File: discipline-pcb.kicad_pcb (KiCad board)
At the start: 2 copper layers, 304.9 x 122.8 mm, 197 parts, among them J1 AVR-ISP-6, SW1 KEYSW, SW10 KEYSW, SW11 KEYSW, SW12 KEYSW, SW13 KEYSW, SW14 KEYSW, SW15 KEYSW, SW16 KEYSW, SW17 KEYSW, SW18 KEYSW, SW19 KEYSW, SW2 KEYSW, SW20 KEYSW, SW21 KEYSW, SW22 KEYSW, SW23 KEYSW, SW24 KEYSW, SW25 KEYSW, SW26 KEYSW, SW27 KEYSW, SW28 KEYSW, SW29 KEYSW, SW3 KEYSW, SW30 KEYSW, SW31 KEYSW, SW32 KEYSW, SW33 KEYSW, SW34 KEYSW, SW35 KEYSW, SW36 KEYSW, SW37 KEYSW, SW38 KEYSW, SW39 KEYSW, SW4 KEYSW, SW40 KEYSW, SW41 KEYSW, SW42 KEYSW, SW43 KEYSW, SW44 KEYSW, SW45 KEYSW, SW46 KEYSW, SW47 KEYSW, SW48 KEYSW, SW49 KEYSW, SW5 KEYSW, SW50 KEYSW, SW51 KEYSW, SW52 KEYSW, SW53 KEYSW, SW54 KEYSW, SW55 KEYSW, SW56 KEYSW, SW57 KEYSW, SW58 KEYSW, SW59 KEYSW, SW6 KEYSW, SW60 KEYSW, SW61 KEYSW, SW62 KEYSW, SW63 KEYSW, SW64 KEYSW, SW65 KEYSW, SW66 KEYSW, SW67 KEYSW, SW68 KEYSW, SW69 KEYSW, SW7 KEYSW, SW70 KEYSW, SW71 KEYSW, SW72 KEYSW, SW73 KEYSW, SW74 KEYSW, SW75 KEYSW, SW76 KEYSW, SW77 KEYSW, SW78 KEYSW, SW8 KEYSW, SW9 KEYSW, U1 ATmega32A-PU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

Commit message: modified the front etch under the 'Discipline' logo
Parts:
- removed the G*** at (155.1, 174.0)
- removed the G*** at (155.1, 168.3)
- added G***: LOGO, discipline-keyboard:my_full_name, F.Cu at (155.2, 169.9)
- added G***: LOGO, discipline-keyboard:rev1.0, F.Cu at (155.2, 172.7)
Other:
- net class Default removed
- board text removed: "1.1"
- board text removed: "7/2/2019 - updated 12/3/2019"
- board text removed: "DISCIPLINE - 65% keyboard assembled with only through hole components"

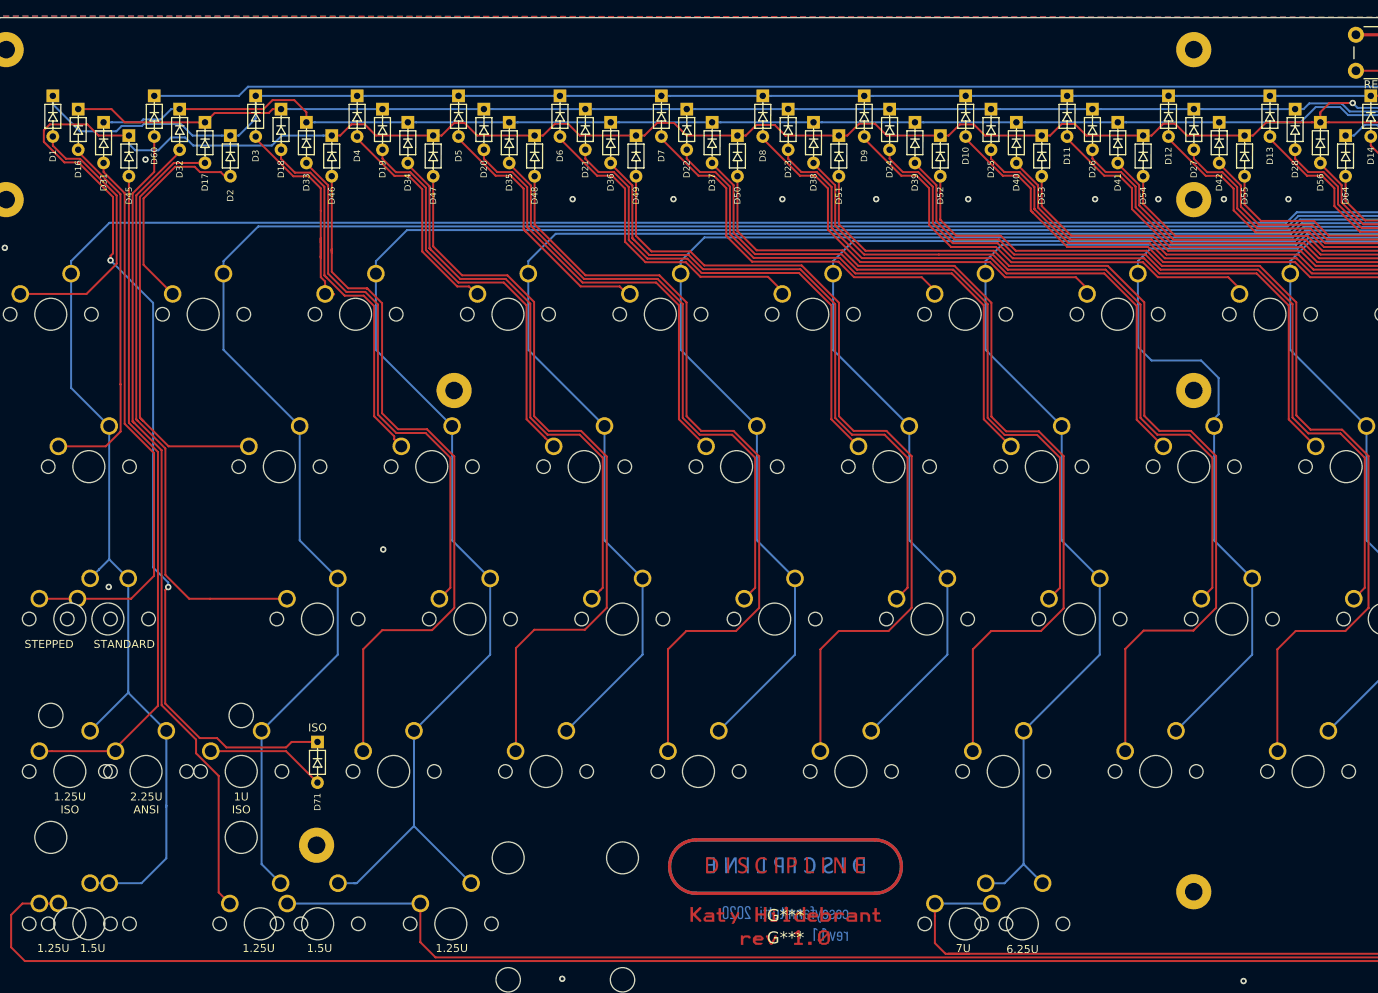
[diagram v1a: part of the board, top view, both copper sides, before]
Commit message: final touches - added copper etch pattern to top of board, added name/version to bottom of board, re-generated gerber files
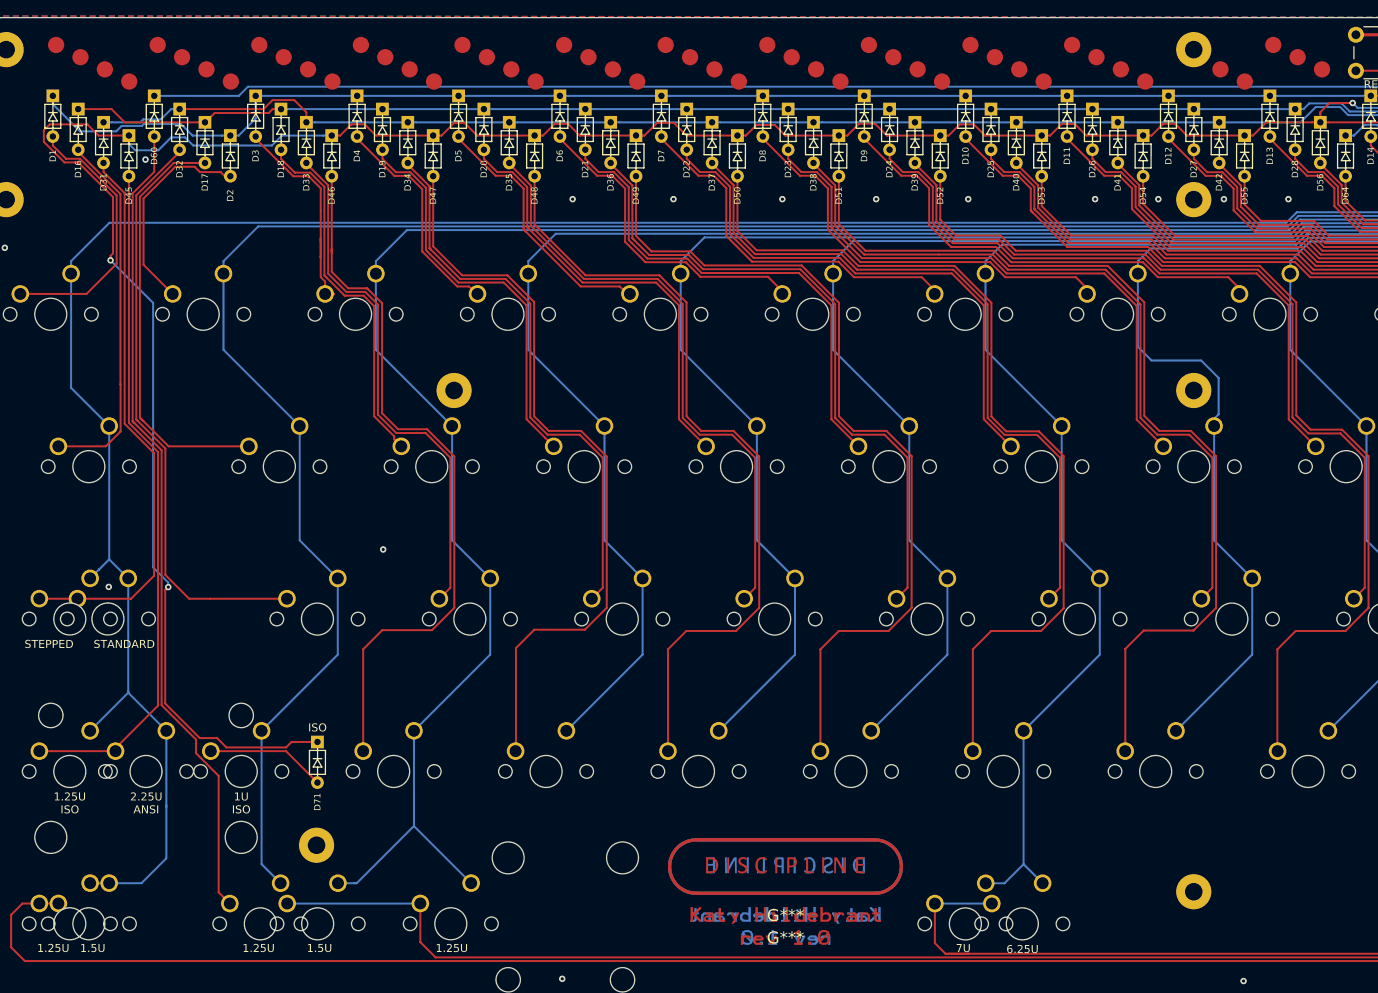
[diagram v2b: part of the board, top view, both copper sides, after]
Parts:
- removed the G*** at (155.2, 174.0) (x2)
- removed the G*** at (155.3, 168.3) (x2)
- removed the G*** at (155.1, 168.3)
- removed the G*** at (155.1, 174.0)
- added G***: LOGO, discipline-keyboard:my_full_name, B.Cu at (155.2, 169.9)
- added G***: LOGO, discipline-keyboard:rev1.0, B.Cu at (155.2, 172.7)
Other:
- rule pad_to_mask_clearance: 0.051 -> 0
